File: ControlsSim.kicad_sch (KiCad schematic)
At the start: 26 parts, among them J2 Accelerator Pot, J3 Brake Button, J5 Motor Contactors, J6 Array Contactors, J7 Rotary Switch, SW2 SW_Rotary2x6

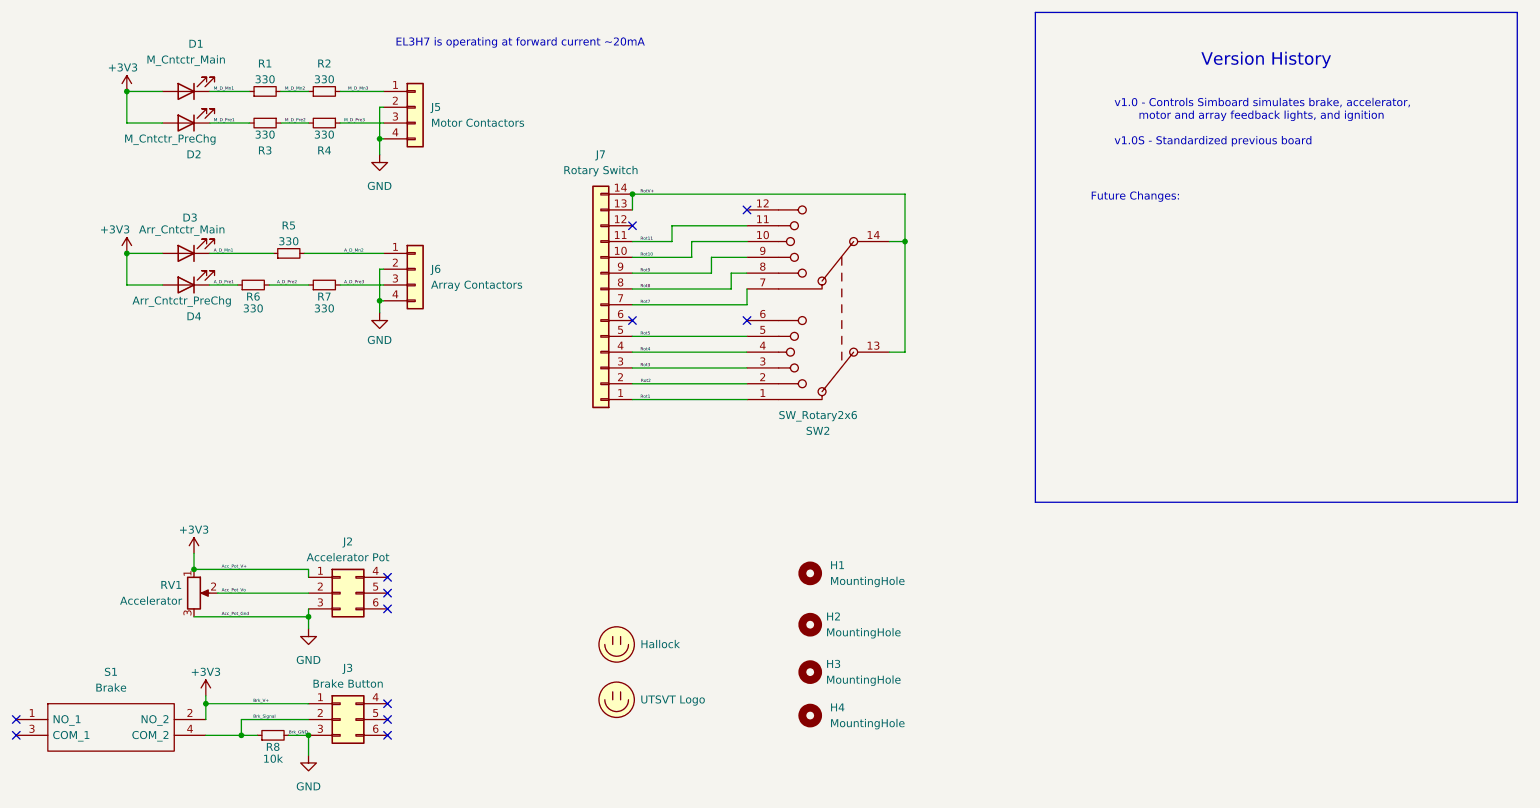
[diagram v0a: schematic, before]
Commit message: Fixed resistor value and layout, fixed labels for rotary encoder.
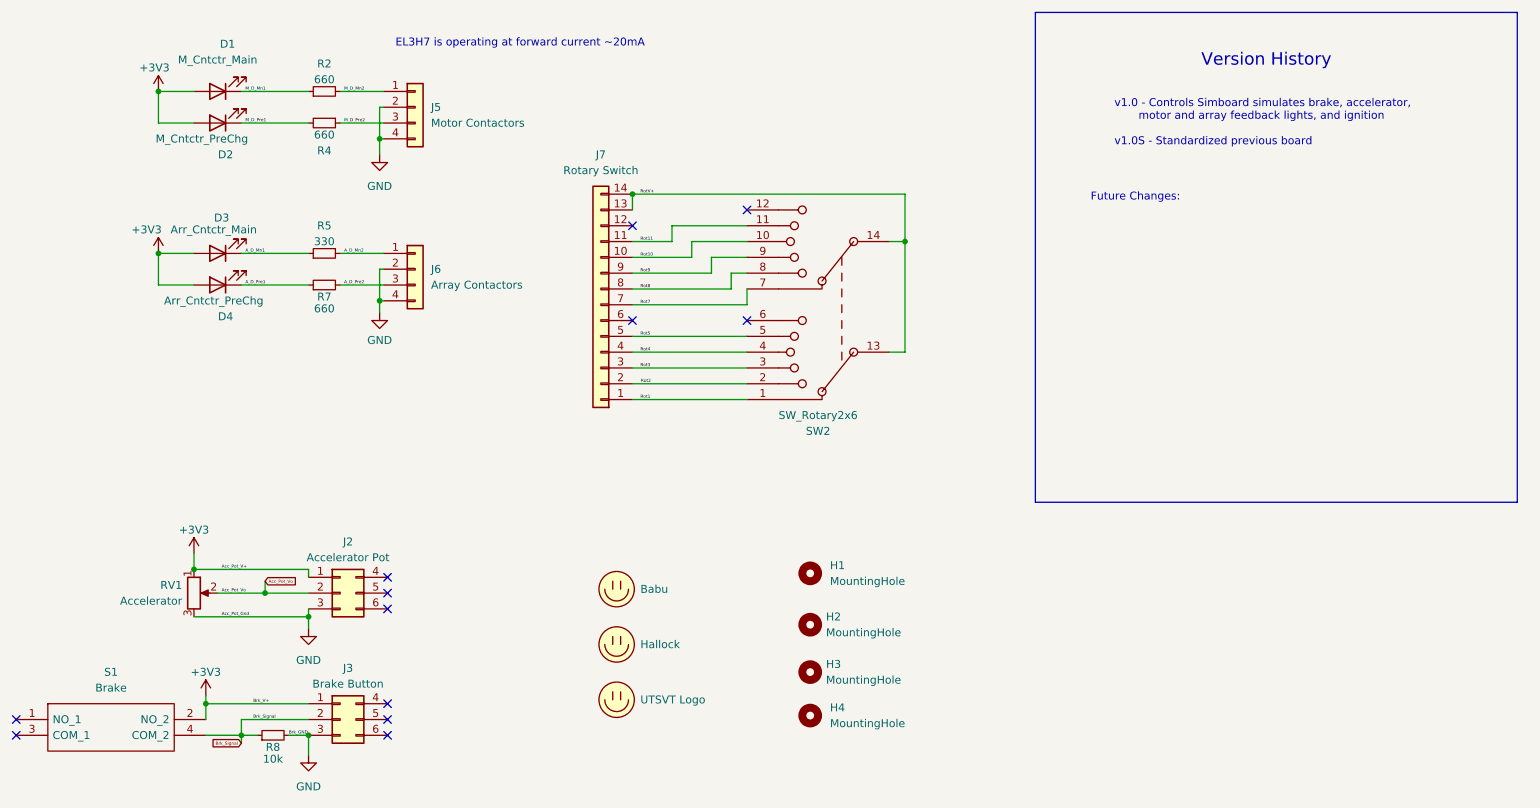
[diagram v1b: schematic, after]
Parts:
- removed R1, R3, R6: 330, Resistor_SMD:R_0805_2012Metric, symbol Device:R_Small
- added LOGO3: Babu, UTSVT_Special:Babu the Builder, symbol utsvt-misc:Logo_Placeholder
- R2, R4, R7: value 330 -> 660
- RV1: footprint Footprints:PTA4543 -> UTSVT_Special:PTA4543
- S1: footprint TS16121295BK260SMTTR -> UTSVT_Special:TS16121295BK260SMTTR
- SW2: footprint Footprints:CK1035 -> UTSVT_Special:CK1035_resized
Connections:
- net A_D_Pre3 is gone; now on net A_D_Pre2: J6.3 (Pin_3), R7.2
- net M_D_Mn3 is gone; now on net M_D_Mn2: J5.1 (Pin_1), R2.2
- net M_D_Pre3 is gone; now on net M_D_Pre2: J5.3 (Pin_3), R4.1
- net A_D_Pre1: now also R7.1
- net A_D_Pre2: no longer R7.1
- net M_D_Mn1: now also R2.1
- net M_D_Mn2: no longer R2.1
- net M_D_Pre1: now also R4.2
- net M_D_Pre2: no longer R4.2
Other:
- moved on the sheet: D1, D2, D3, D4, R5

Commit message: Updated BOM
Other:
- note added: "Future Changes: * Combine this board with dashboard"
- note added: "v1.0 - Controls Simboard simulates brake, accelerator, motor and array feedback lights, and ignition v1.0S - Standardized previous board v2.0s - Updated the board to better fit the new rotary encoder footprint"
- note removed: "Future Changes:"
- note removed: "v1.0 - Controls Simboard simulates brake, accelerator, motor and array feedback lights, and ignition v1.0S - Standardized previous board"
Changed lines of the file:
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@@
     (stroke (width 0) (type default))
   )
-  (text "v1.0 - Controls Simboard simulates brake, accelerator,\n	   motor and array feedback lights, and ignition\n\nv1.0S - Standardized previous board"
+  (text "v1.0 - Controls Simboard simulates brake, accelerator,\n	   motor and array feedback lights, and ignition\n\nv1.0S - Standardized previous board\n\nv2.0s - Updated the board to better fit the new rotary \n        encoder footprint"
     (at 200.66 55.88 0)
     (effects (font (size 1.27 1.27)) (justify left bottom))
   )
-  (text "Future Changes:" (at 196.85 64.77 0)
+  (text "Future Changes:\n\n* Combine this board with dashboard"
+    (at 196.85 64.77 0)
     (effects (font (size 1.27 1.27)) (justify left bottom))
   )
